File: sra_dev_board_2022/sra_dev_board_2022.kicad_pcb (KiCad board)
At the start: 2 copper layers, 81.2 x 92.7 mm, 177 parts, among them J1 Conn_01x19_Male, J11 Conn_01x05_Male, J12 Conn_01x05_Male, J13 Conn_01x05_Male, J2 Conn_01x03_Male, J3 Conn_01x03_Male, J4 Conn_01x03_Male, J5 Conn_01x19_Male, J6 DCJ200-10-A-XX-X_REVA, J7 Conn_01x06_Male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

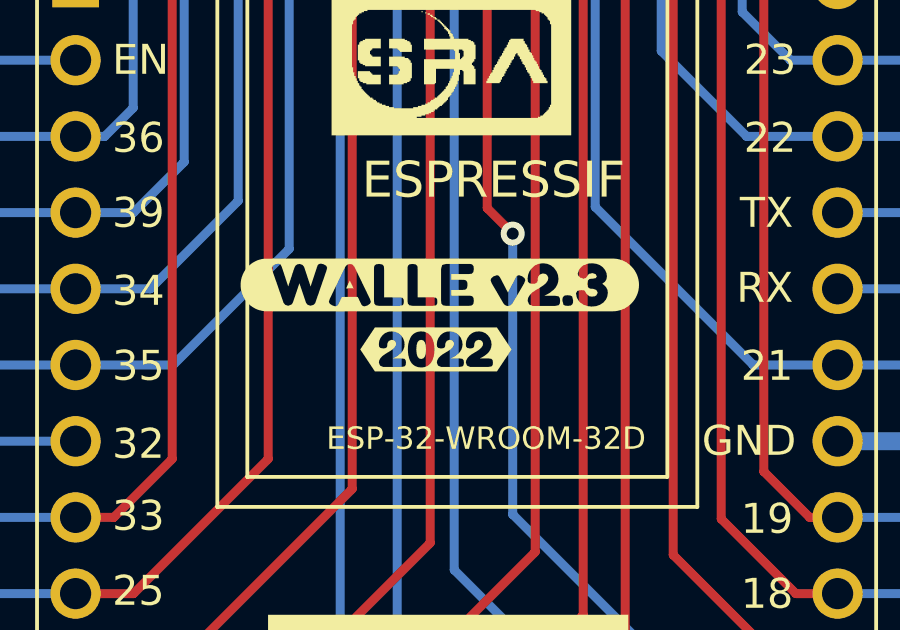
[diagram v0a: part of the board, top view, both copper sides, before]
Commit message: Added Interactive BOM, SMT pick place files
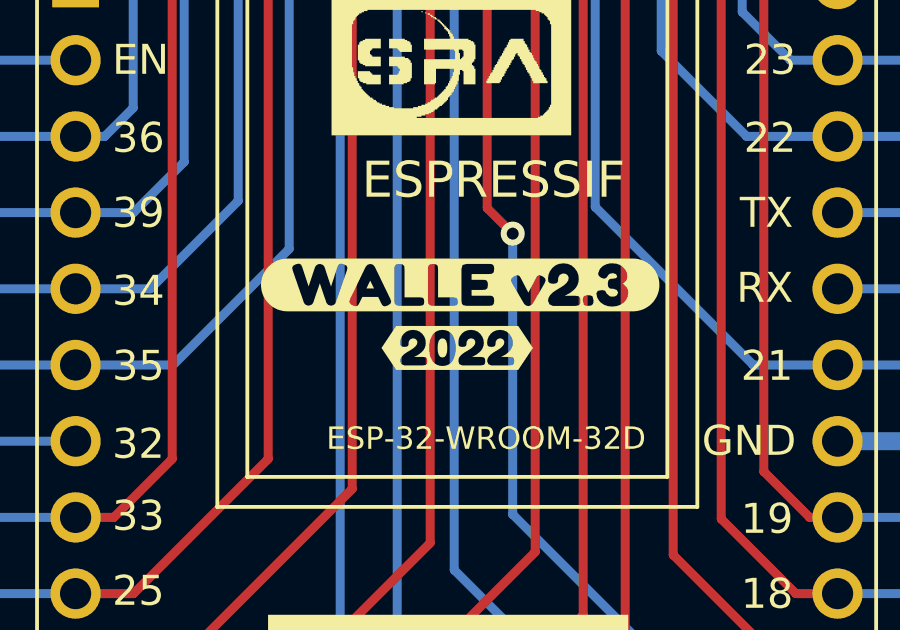
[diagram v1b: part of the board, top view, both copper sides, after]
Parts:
- moved kibuzzard-61F6AD42 0.71 mm to (125.9, 85.0) (x2)
- moved kibuzzard-61F6AD1B 0.68 mm to (126.0, 82.9) (x2)
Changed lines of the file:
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@@
   )
   (footprint "kibuzzard-61F6AD1B" (layer "F.Cu")
-    (at 125.32 82.9)
+    (at 126 82.9)
     (descr "Converted using: scripting")
     (tags "kb_params=7b27416c69676e6d656e7443686f696365273a202743656e746572272c20274361704c65667443686f696365273a202728272c2027436170526967687443686f696365273a202729272c2027466f6e74436f6d626f426f78273a2027467265646f6b614f6e65272c20274865696768744374726c273a2027312e32272c20274d756c74694c696e6554657874273a202757414c4c452076322e33272c202750616464696e67426f74746f6d4374726c273a202732272c202750616464696e674c6566744374726c273a202732272c202750616464696e6752696768744374726c273a202732272c202750616464696e67546f704374726c273a202732272c202757696474684374726c273a202731277d")
@@
   )
   (footprint "kibuzzard-61F6AD42" (layer "F.Cu")
-    (at 125.19 85.05)
+    (at 125.9 85)
     (descr "Converted using: scripting")
     (tags "kb_params=7b27416c69676e6d656e7443686f696365273a202743656e746572272c20274361704c65667443686f696365273a20273c272c2027436170526967687443686f696365273a20273e272c2027466f6e74436f6d626f426f78273a2027467265646f6b614f6e65272c20274865696768744374726c273a202731272c20274d756c74694c696e6554657874273a202732303232272c202750616464696e67426f74746f6d4374726c273a202732272c202750616464696e674c6566744374726c273a202732272c202750616464696e6752696768744374726c273a202732272c202750616464696e67546f704374726c273a202732272c202757696474684374726c273a202731277d")
@@
   )
   (footprint "kibuzzard-61F6AD1B" (layer "B.Cu")
-    (at 125.32 82.9 180)
+    (at 126 82.9 180)
     (descr "Converted using: scripting")
     (tags "kb_params=7b27416c69676e6d656e7443686f696365273a202743656e746572272c20274361704c65667443686f696365273a202728272c2027436170526967687443686f696365273a202729272c2027466f6e74436f6d626f426f78273a2027467265646f6b614f6e65272c20274865696768744374726c273a2027312e32272c20274d756c74694c696e6554657874273a202757414c4c452076322e33272c202750616464696e67426f74746f6d4374726c273a202732272c202750616464696e674c6566744374726c273a202732272c202750616464696e6752696768744374726c273a202732272c202750616464696e67546f704374726c273a202732272c202757696474684374726c273a202731277d")
@@
   )
   (footprint "kibuzzard-61F6AD42" (layer "B.Cu")
-    (at 125.19 85.05 180)
+    (at 125.9 85 180)
     (descr "Converted using: scripting")
     (tags "kb_params=7b27416c69676e6d656e7443686f696365273a202743656e746572272c20274361704c65667443686f696365273a20273c272c2027436170526967687443686f696365273a20273e272c2027466f6e74436f6d626f426f78273a2027467265646f6b614f6e65272c20274865696768744374726c273a202731272c20274d756c74694c696e6554657874273a202732303232272c202750616464696e67426f74746f6d4374726c273a202732272c202750616464696e674c6566744374726c273a202732272c202750616464696e6752696768744374726c273a202732272c202750616464696e67546f704374726c273a202732272c202757696474684374726c273a202731277d")

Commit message: SRA Board, MPU, LSA Kicad, Gerber files updated
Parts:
- removed the G*** at (125.6, 99.9) (x2)
- removed kibuzzard-61F6A2FC (x2): G***, kibuzzard-61F6A2FC
- removed kibuzzard-61F6A310 (x2): G***, kibuzzard-61F6A310
- removed kibuzzard-61F6A5AC: G***, kibuzzard-61F6A5AC
- removed kibuzzard-61F6A703: G***, kibuzzard-61F6A703
- removed kibuzzard-61F6A70A: G***, kibuzzard-61F6A70A
- removed kibuzzard-61F7B758: G***, kibuzzard-61F7B758
- removed the kibuzzard-61F7D60F at (138.1, 46.5)
- removed kibuzzard-61F7F3F0: G***, kibuzzard-61F7F3F0
- removed kibuzzard-61F7F991: G***, kibuzzard-61F7F991
- added G***: LOGO, logos:sra_board_github_qr_code, F.Cu at (125.9, 98.3)
- added G***: LOGO, logos:sra_board_github_qr_code, B.Cu at (125.9, 98.4)
- added J10: Conn_01x03_Male, pin_header_connectors:1X03, F.Cu at (144.1, 56.5)
- added kibuzzard-620CE59A: G***, kibuzzard-620CE59A, F.Cu at (116.3, 46.0)
- added kibuzzard-620D3625: G***, kibuzzard-620D3625, F.Cu at (140.9, 54.3)
- added kibuzzard-620D363E: G***, kibuzzard-620D363E, F.Cu at (147.1, 54.3)
- added kibuzzard-620D3646: G***, kibuzzard-620D3646, F.Cu at (143.8, 54.3)
- added kibuzzard-620D3ACF: G***, kibuzzard-620D3ACF, F.Cu at (144.1, 67.7)
- added kibuzzard-620D3ACF: G***, kibuzzard-620D3ACF, B.Cu at (144.1, 67.7)
- added kibuzzard-620D3AFB: G***, kibuzzard-620D3AFB, F.Cu at (146.6, 68.3)
- added kibuzzard-620D3AFB: G***, kibuzzard-620D3AFB, B.Cu at (146.6, 68.3)
- added kibuzzard-620D3FD3: G***, kibuzzard-620D3FD3, F.Cu at (139.4, 59.2)
- added kibuzzard-620D3FD3: G***, kibuzzard-620D3FD3, B.Cu at (139.3, 59.2)
- added kibuzzard-620D3FE5: G***, kibuzzard-620D3FE5, F.Cu at (139.4, 56.5)
- added kibuzzard-620D4024: G***, kibuzzard-620D4024, F.Cu at (139.4, 61.9)
- added kibuzzard-620D4024: G***, kibuzzard-620D4024, B.Cu at (139.4, 61.9)
- added kibuzzard-620D404F: G***, kibuzzard-620D404F, F.Cu at (139.3, 64.9)
- added kibuzzard-620D4F5E: G***, kibuzzard-620D4F5E, B.Cu at (139.3, 64.9)
- added kibuzzard-620D4F84: G***, kibuzzard-620D4F84, B.Cu at (139.3, 56.5)
- moved kibuzzard-61F7D5C6 8.94 mm to (126.7, 50.9)
- moved kibuzzard-61F7CB17 8.37 mm to (126.5, 42.4)
- moved kibuzzard-61F6A2E5 2.59 mm to (141.5, 68.7)
- moved kibuzzard-61F6A2E5 2.57 mm to (141.4, 68.7)
- moved J4 2.47 mm to (144.1, 62.1)
- moved J2 2.47 mm to (144.1, 59.3)
- moved J3 2.47 mm to (144.1, 64.9)
- moved kibuzzard-61F6A6E8 1.43 mm to (150.0, 61.2)
- moved G*** 1.38 mm to (148.0, 73.3)
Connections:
- SW1 pad 2: /4 -> GND
- SW1 pad 3: GND -> unconnected-(SW1-Pad3)
- SW2 pad 2: /2 -> GND
- SW2 pad 3: GND -> unconnected-(SW2-Pad3)
- SW3 pad 2: /17 -> GND
- SW3 pad 3: GND -> unconnected-(SW3-Pad3)
- SW4 pad 2: /16 -> GND
- SW4 pad 3: GND -> unconnected-(SW4-Pad3)
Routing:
- net /15: track 4.99 -> 67.8 mm
- net GND: track 119.9 -> 105.9 mm, vias 36 -> 40
- net /17: track 52.2 -> 48.2 mm
- net /21: track 70.9 -> 74.4 mm
- net /5: track 51.2 -> 48.2 mm
- net /2: track 65.6 -> 62.6 mm
- net /4: track 68.5 -> 65.6 mm
- net /18: track 44.3 -> 41.5 mm
- net /16: track 62.2 -> 59.5 mm
- net /19: track 36.9 -> 34.2 mm
- net /5V: track 102.2 -> 104.8 mm
- net /33: track 89.1 -> 87.4 mm
- net /14: track 113.5 -> 114.7 mm
- net /13: track 114.4 -> 113.6 mm
- net /26: track 90.4 -> 89.9 mm
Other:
- board text added: "Arm"
- board text added: "Base"
- board text added: "Elbow"
- board text added: "Gripper"
- board text added: "sravjti.in"

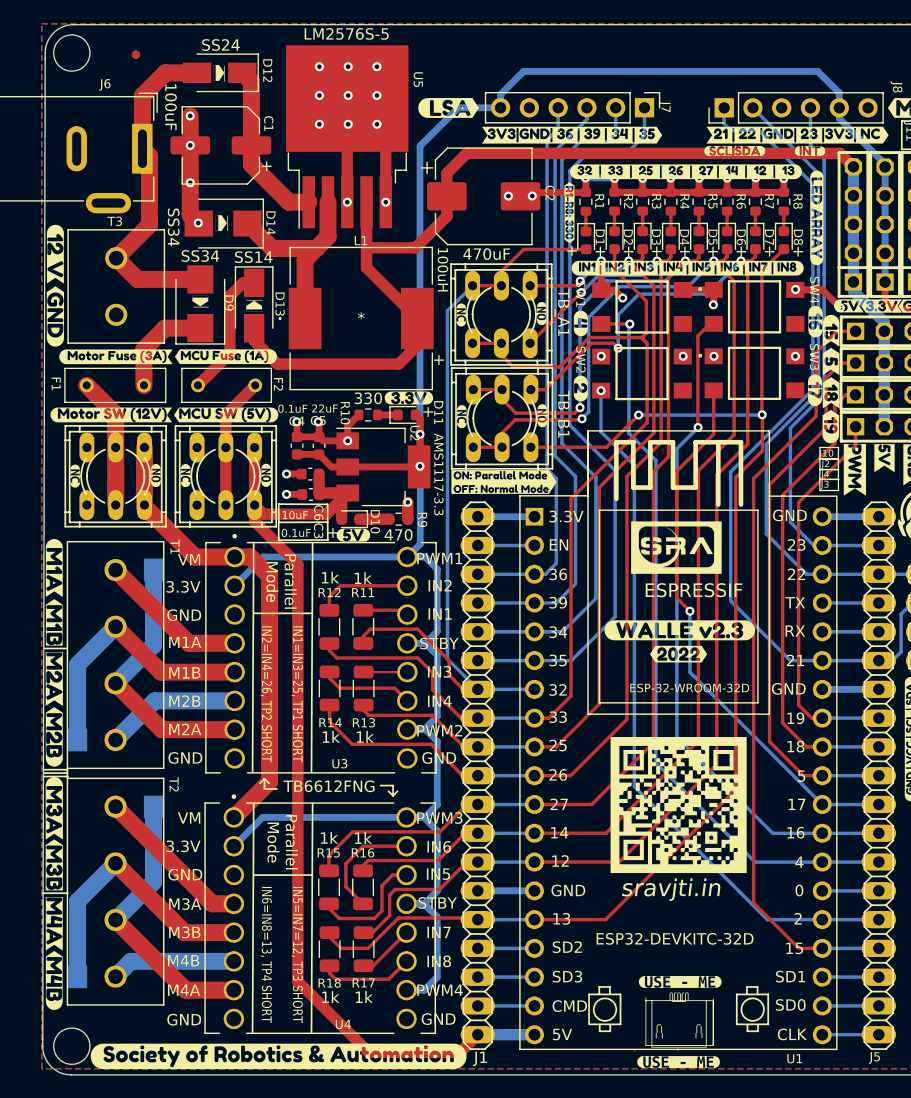
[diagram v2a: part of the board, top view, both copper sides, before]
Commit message: Modify routing according to new schematic
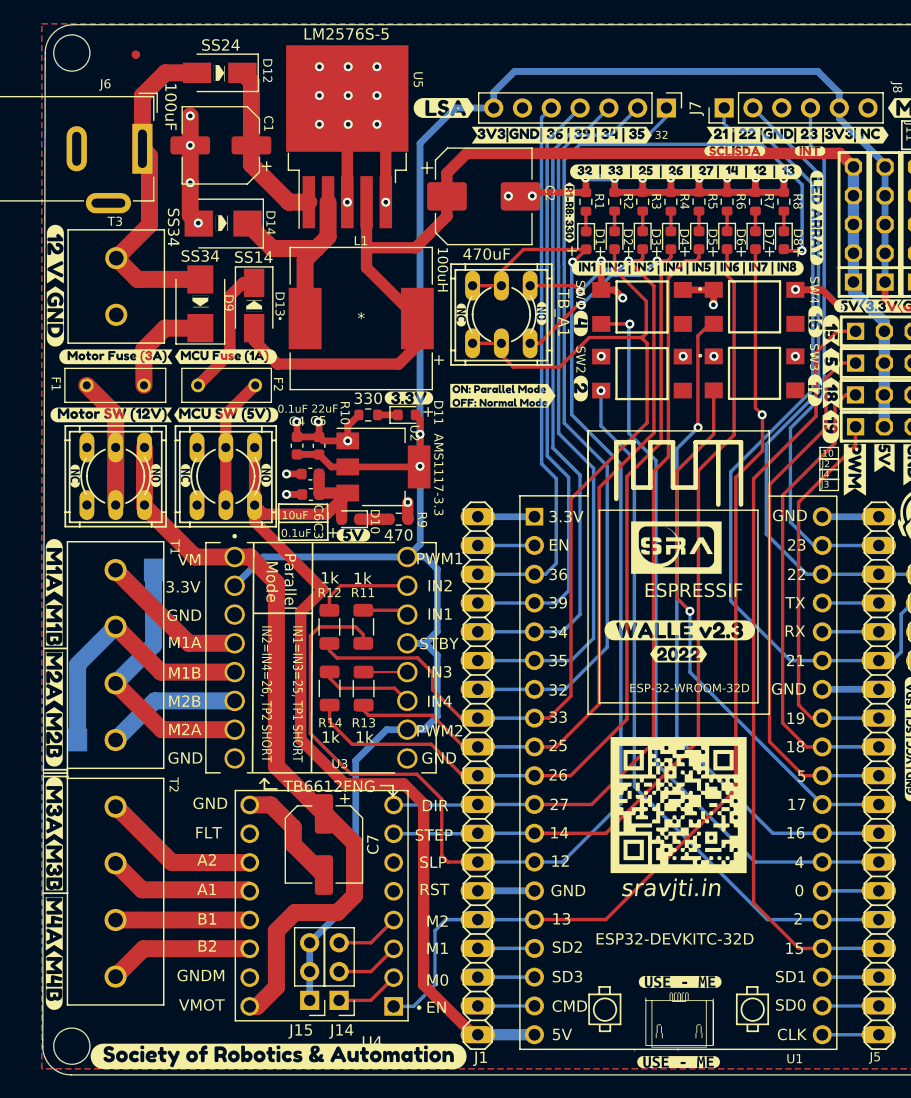
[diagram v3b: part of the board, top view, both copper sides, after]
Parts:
- removed R15, R16, R17, R18: 1k, Resistor_SMD:R_1206_3216Metric
- removed TB_B1: SW_Push_DPDT, dpdt_tht:dpdt_sw_2x03_tht
- removed TP3, TP4: TestPoint, testpoint_pad:pad_1,27-2,54_smd
- removed the kibuzzard-61F67ED2 at (106.8, 64.0)
- removed the kibuzzard-61F6808A at (113.9, 64.0)
- added C7: 100uF, Capacitor_SMD:CP_Elec_6.3x7.7, F.Cu at (94.6, 101.8)
- added J14: Conn_01x03_Male, Connector_PinHeader_2.54mm:PinHeader_1x03_P2.54mm_Vertical, F.Cu at (95.9, 115.6)
- added J15: Conn_01x03_Male, Connector_PinHeader_2.54mm:PinHeader_1x03_P2.54mm_Vertical, F.Cu at (93.3, 115.6)
- J7: value Conn_01x06_Male -> Conn_01x07_Male; footprint Connector_PinHeader_2.54mm:PinHeader_1x06_P2.54mm_Vertical -> Connector_PinHeader_2.54mm:PinHeader_1x07_P2.54mm_Vertical
- U4: value TB6612FNG -> DRV8825_STEPPER_MOTOR_DRIVER_CARRIER; footprint motor_driver:TB6612FNG_2 -> stepper_motor_driver:IC_DRV8825_STEPPER_MOTOR_DRIVER_CARRIER
- moved kibuzzard-61F7BB7D 7.61 mm to (110.4, 62.2)
- moved J7 1.94 mm to (124.8, 36.8)
- moved U4 1.11 mm to (94.4, 107.2), turned to 180 degrees
- moved kibuzzard-61F7C12E 0.90 mm to (115.6, 39.2)
- moved kibuzzard-61F7C0C2 0.40 mm to (105.2, 36.8)
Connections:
- D1 pad 2: /32 -> /12
- D7 pad 2: /12 -> /13
- D8 pad 2: /13 -> /32
- J7 pad 1: /35 -> /32
- J7 pad 2: /34 -> /35
- J7 pad 3: /39 -> /34
- J7 pad 4: /36 -> /39
- J7 pad 5: GND -> /36
- J7 pad 6: /3V3 -> GND
- R11 pad 1: /32 -> /12
- T2 pad 1: /OUT1B -> /A_2
- T2 pad 2: /OUT2B -> /A_1
- T2 pad 3: /OUT3B -> /B_1
- T2 pad 4: /OUT4B -> /B_2
- TB_A1 pad 1: /32 -> /12
- TB_A1 pad 2: /32 -> /12
- U4 pad 1: /12V_P -> /13
- U4 pad 10: /3V3 -> unconnected-(U4-Pad10)
- U4 pad 11: Net-(R18-Pad2) -> /A_2
- U4 pad 12: Net-(R17-Pad2) -> /A_1
- U4 pad 13: /3V3 -> /B_1
- U4 pad 14: Net-(R15-Pad2) -> /B_2
- U4 pad 15: Net-(R16-Pad2) -> GND
- U4 pad 16: /3V3 -> /12V_P
- U4 pad 2: /3V3 -> /M0
- U4 pad 3: GND -> /M1
- U4 pad 4: /OUT1B -> /M2
- U4 pad 5: /OUT2B -> unconnected-(U4-Pad5)
- U4 pad 6: /OUT4B -> unconnected-(U4-Pad6)
- U4 pad 7: /OUT3B -> /14
- U4 pad 8: GND -> /27
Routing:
- net /27: track 110.7 -> 71.9 mm, vias 2 -> 0
- net /14: track 114.7 -> 76.4 mm, vias 2 -> 0
- net /12V_P: track 41.4 -> 66.4 mm
- net /32: track 68.7 -> 93.6 mm, vias 0 -> 1
- net /OUT3B: track 24.4 -> 0.00 mm
- net /OUT2B: track 24.4 -> 0.00 mm
- net /13: track 113.6 -> 90.0 mm, vias 2 -> 1
- net /3V3: track 240.1 -> 217.4 mm
- net /OUT1B: track 14.0 -> 0.00 mm
- net /A_2: track 0.00 -> 13.9 mm
- net /B_2: track 0.00 -> 12.9 mm
- net /A_1: track 0.00 -> 12.9 mm
- net /B_1: track 0.00 -> 11.8 mm
- net /OUT4B: track 11.0 -> 0.00 mm
- net Net-(R15-Pad2): track 10.5 -> 0.00 mm
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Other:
- board text added: "A1"
- board text added: "A2"
- board text added: "B1"
- board text added: "B2"
- board text added: "DIR"
- board text added: "FLT"
- board text added: "GNDM"
- board text added: "M0"
- board text added: "M1"
- board text added: "M2"
- board text added: "RST"
- board text added: "SLP"
- board text added: "STEP"
- board text added: "VMOT"
- board text removed: "IN5=IN7=12, TP3 SHORT IN6=IN8=13, TP4 SHORT"

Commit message: modify silkscreen
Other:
- board text removed: "IN5"
- board text removed: "IN6"
- board text removed: "IN7"
- board text removed: "IN8"
- board text removed: "M3B"
- board text removed: "M4B"
- board text removed: "PWM3"
- board text removed: "PWM4"
- board text removed: "TP3"
- board text removed: "TP4"
